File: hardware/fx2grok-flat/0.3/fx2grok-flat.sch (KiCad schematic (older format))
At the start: 36 parts, among them IC1 CY7C68013A-56, J1 Conn, P1 pkl_USB_OTG, U1 3.3V, U2 USBLC6-2, U3 IP425x-4-TTL, U4 IP425x-4-TTL, U5 24LC00, U6 IP425x-4-TTL, X1 24MHz

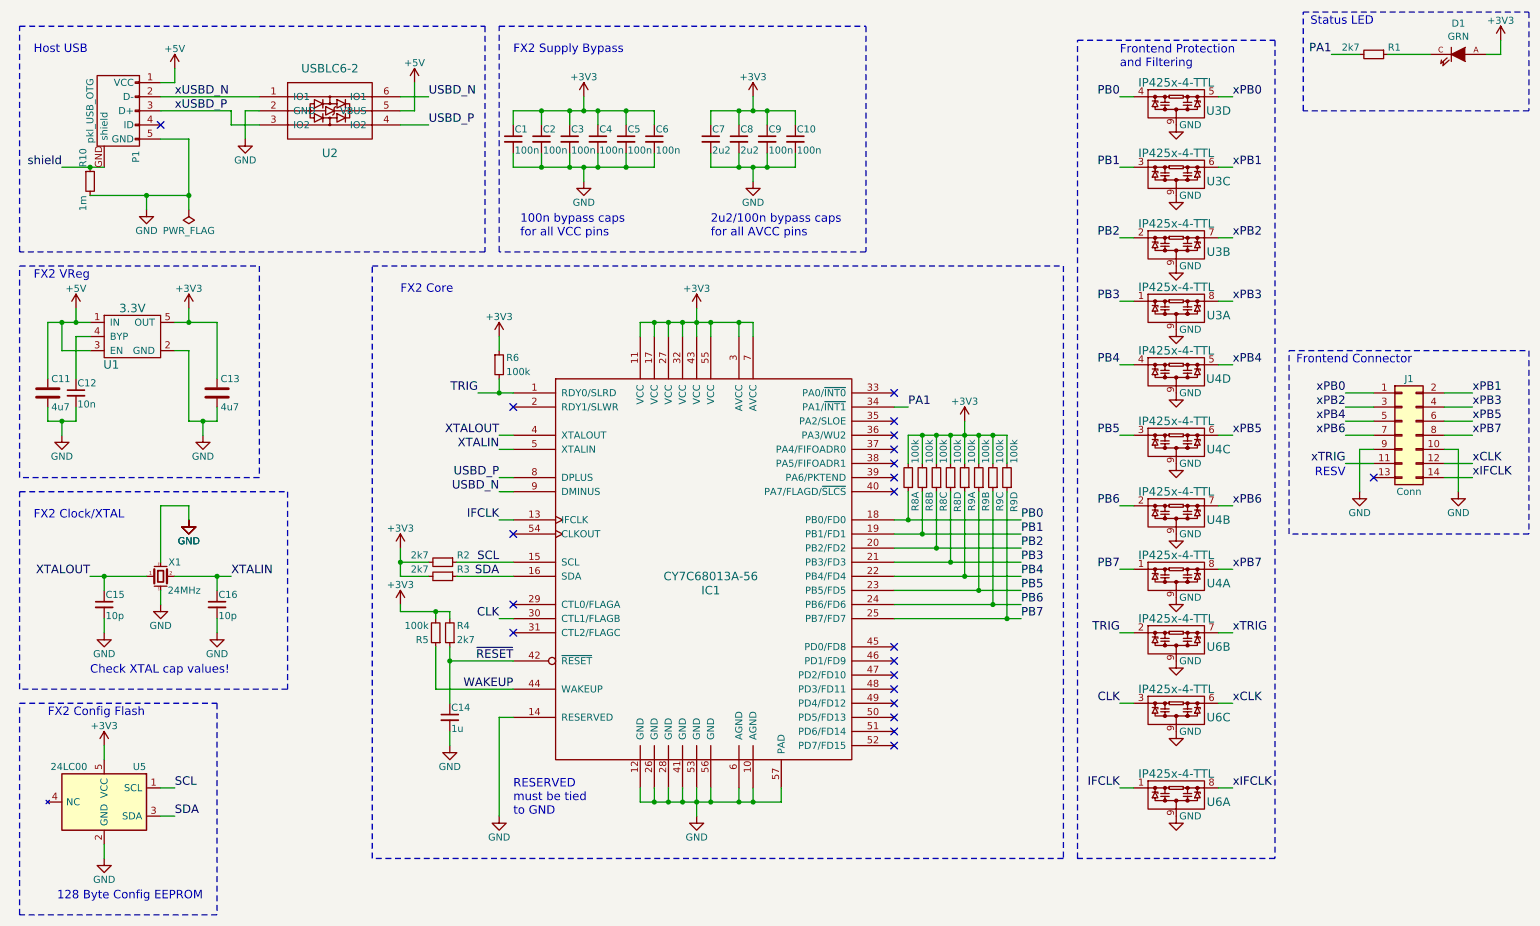
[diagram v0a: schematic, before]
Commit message: Added TRIG2 (RDY1/SLWR) as per @StefanBruens request. :D
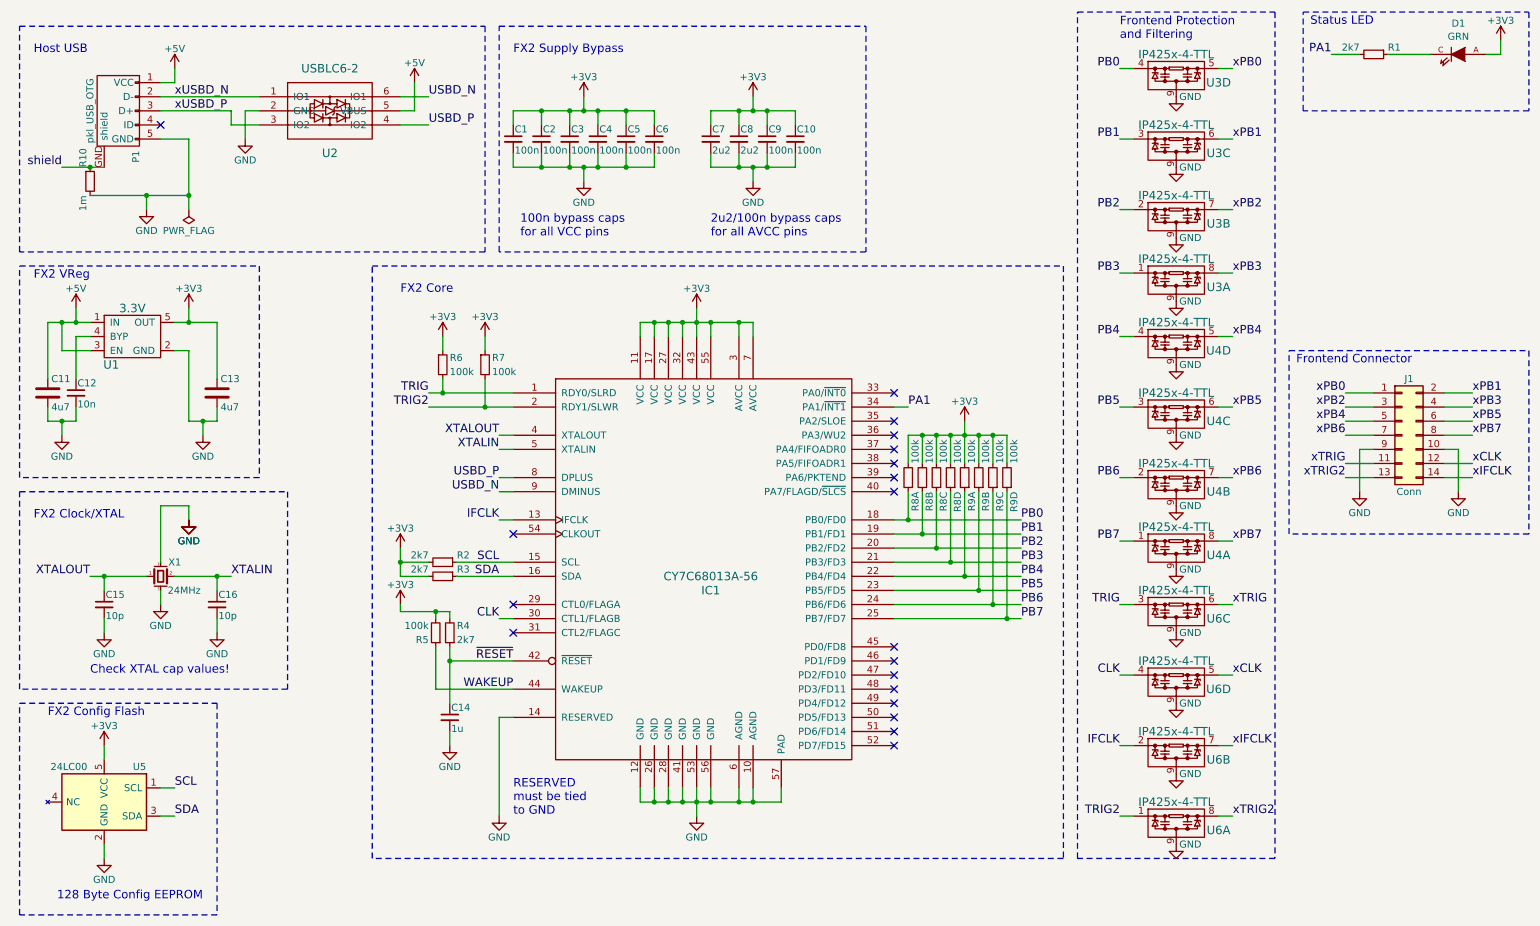
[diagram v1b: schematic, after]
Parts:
- added R7: 100k, pkl_dipol:R_0402, symbol pkl_device:pkl_R_Small
- added unit 4 of U6
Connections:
- net +3V3: now also R7.1
- net CLK: now also U6.4; no longer U6.3
- net GND: now also U6.9
- net IFCLK: now also U6.2; no longer U6.1
- net TRIG: now also U6.3; no longer U6.2
- net xCLK: now also U6.5; no longer U6.6
- net xIFCLK: now also U6.7; no longer U6.8
- net xTRIG: now also U6.6; no longer U6.7
- net TRIG2: now reaches IC1.2 (RDY1/SLWR)
- net TRIG2: now also U6.1, R7.2
- net xTRIG2: now reaches J1.13 (Pin_13)
- net xTRIG2: now also U6.8
- no-connect marks 21 -> 19
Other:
- note removed: "RESV"
- moved on the sheet: R6, U3A, U3B, U3C, U3D, U4A, U4B, U4C, U4D, U6A, U6B, U6C
